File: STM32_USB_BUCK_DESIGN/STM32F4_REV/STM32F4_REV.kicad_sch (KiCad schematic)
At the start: 5 parts

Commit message: work going on ckt-desgin
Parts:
- added C? (x5): 100n, symbol Device:C_Small
- added C?: 4u7, symbol Device:C_Small
- added C?: 1u, symbol Device:C_Small
- added C? (x2): 12pF, symbol Device:C_Small
- added C?: 1n, symbol Device:C_Small
- added D?: LED, symbol Device:LED
- added L?: 39h, symbol pspice:INDUCTOR
- added R?: 47, symbol Device:R_Small
- added R?: 1K5, symbol Device:R_Small
- added U?: mp2359, symbol Prashant_library:mp2359
- added Y?: 16Mhz, symbol Device:Crystal_GND24_Small
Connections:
- net +3.3V: now also C?.1, C?.1, C?.1, C?.1, C?.1, C?.1, L?.1
- net GND: now also C?.2, C?.2, C?.2, C?.2, C?.2, C?.2, C?.2, C?.2, C?.2, C?.2, D?.1 (K), U?.2 (GND), Y?.2, Y?.4
- net HSE_IN: now also C?.1, Y?.1
- net HSE_ON: now also R?.1
- net LED_STATUS: now also R?.1
- new net: C?.1, R?.2, Y?.3
- new net: D?.2 (A), R?.2
- new net +3.3VA: C?.1, C?.1, L?.2
- new net BUCK_BST: U?.1 (BST)
- new net BUCK_EN: U?.4 (EN)
- new net BUCK_FB: U?.3 (FB)
- new net BUCK_IN: U?.5 (IN)
- new net BUCK_SW: U?.6 (SW)
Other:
- note added: "CLoad = 2*(CL - Cstray)"
- moved on the sheet: R?, SW?

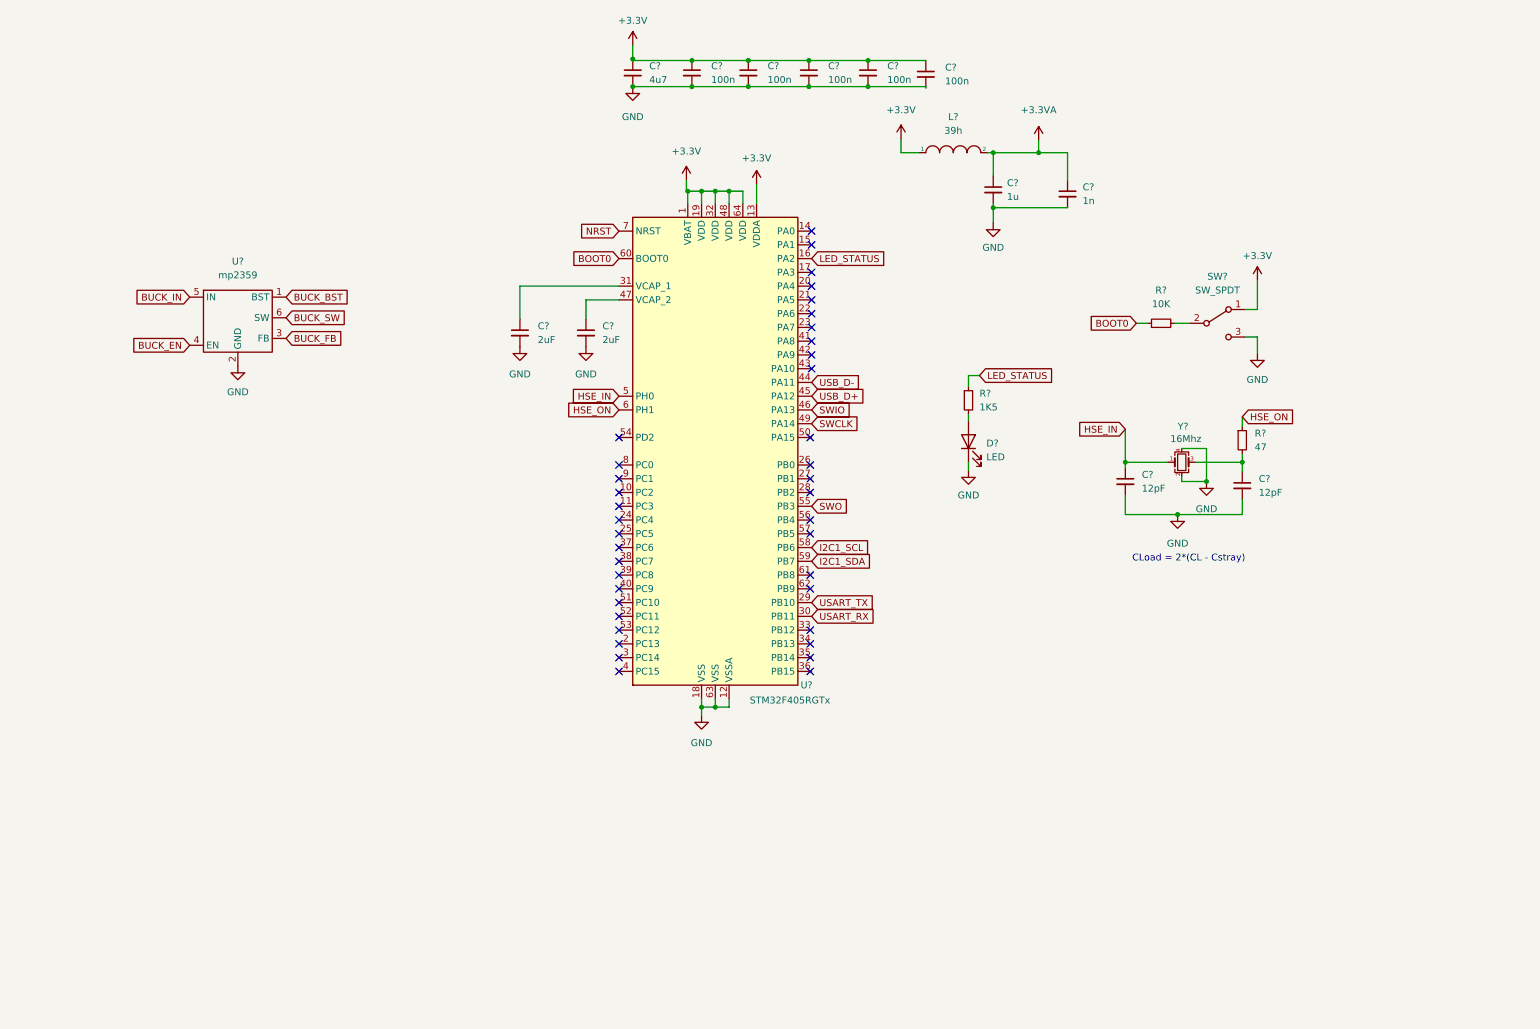
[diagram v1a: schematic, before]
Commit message: design of STM32_USB_BUCK_DESIGN
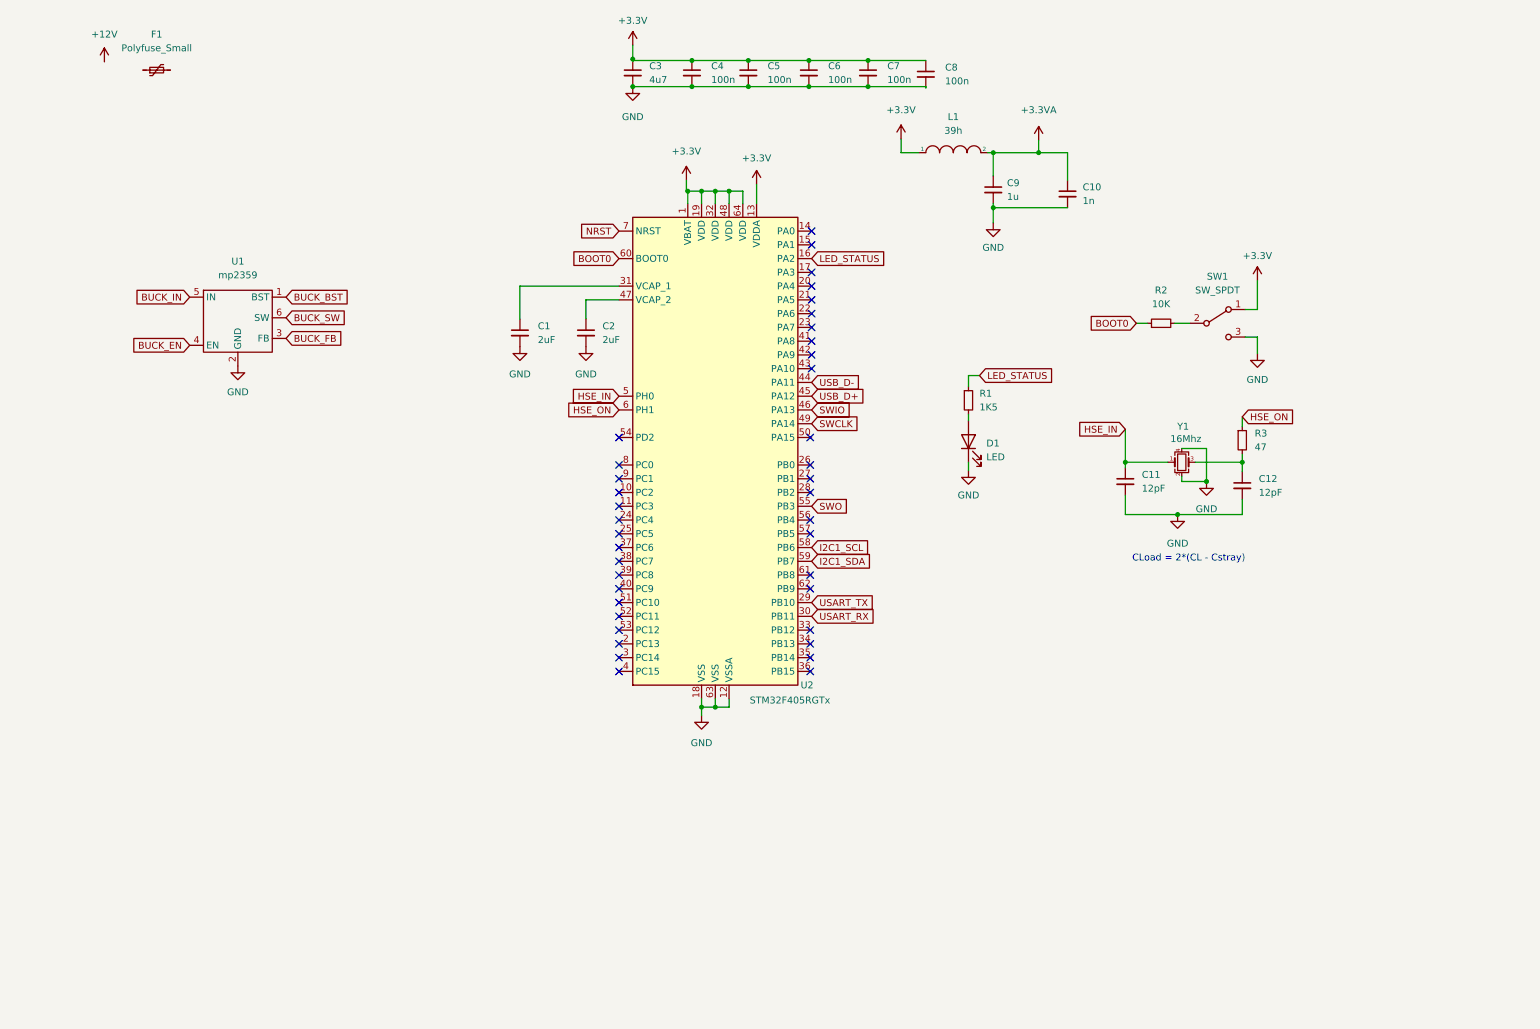
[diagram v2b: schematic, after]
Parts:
- added F1: Polyfuse_Small, symbol Device:Polyfuse_Small
- gave numbers to parts that had none: 21

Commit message: Kam vairaxa
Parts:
- added C1, C2, C3: 10u, Capacitor_SMD:C_1206_3216Metric, symbol Device:C_Small
- added C4: 10n, Capacitor_SMD:C_0603_1608Metric, symbol Device:C_Small
- added D1, D2, D3: B5819W, Diode_SMD:D_SOD-123, symbol Device:D_Schottky_Small
- added D5: LED_Small, LED_SMD:LED_0603_1608Metric, symbol Device:LED_Small
- added FB1: 600 @ 600 MHz, Inductor_SMD:L_0805_2012Metric, symbol Device:FerriteBead_Small
- added H1, H2, H3, H4: MountingHole_Pad, MountingHole:MountingHole_4.3mm_M4_Pad_Via, symbol Mechanical:MountingHole_Pad
- added J1: USB_B_Micro, Connector_USB:USB_Micro-B_Amphenol_10104110_Horizontal, symbol Connector:USB_B_Micro
- added J2: Screw_Terminal_01x02, TerminalBlock_Phoenix:TerminalBlock_Phoenix_PT-1,5-2-3.5-H_1x02_P3.50mm_Horizontal, symbol Connector:Screw_Terminal_01x02
- added J3, J5: Conn_01x04, Connector_Molex:Molex_PicoBlade_53048-0410_1x04_P1.25mm_Horizontal, symbol Connector_Generic:Conn_01x04
- added J4: Conn_02x05_Odd_Even, Connector_PinSocket_1.27mm:PinSocket_2x05_P1.27mm_Vertical_SMD, symbol Connector_Generic:Conn_02x05_Odd_Even
- added L2: 10u, symbol Device:L_Small
- added R10: 270, symbol Device:R_Small
- added R11: 1K, symbol Device:R_Small
- added R4: 100K, symbol Device:R_Small
- added R5: 68K, symbol Device:R_Small
- added R6, R7: 2K2, symbol Device:R_Small
- added R8: 47K, symbol Device:R_Small
- added R9: 15K, symbol Device:R_Small
- added U3: USBLC6-2SC6, Package_TO_SOT_SMD:SOT-23-6, symbol Power_Protection:USBLC6-2SC6
- C10: renamed from C8; footprint (none) -> Capacitor_SMD:C_0603_1608Metric
- C11: renamed from C9; footprint (none) -> Capacitor_SMD:C_0603_1608Metric
- C12: renamed from C10; footprint (none) -> Capacitor_SMD:C_0603_1608Metric
- C13: renamed from C1; value 2uF -> 2u2; footprint (none) -> Capacitor_SMD:C_0603_1608Metric
- C14: renamed from C2; value 2uF -> 2u2; footprint (none) -> Capacitor_SMD:C_0603_1608Metric
- C15: renamed from C11; footprint (none) -> Capacitor_SMD:C_0805_2012Metric
- C16: renamed from C12; footprint (none) -> Capacitor_SMD:C_0805_2012Metric
- C5: renamed from C3; footprint (none) -> Capacitor_SMD:C_0805_2012Metric
- C6: renamed from C4; footprint (none) -> Capacitor_SMD:C_0603_1608Metric
- C7: renamed from C5; footprint (none) -> Capacitor_SMD:C_0603_1608Metric
- C8: renamed from C6; footprint (none) -> Capacitor_SMD:C_0603_1608Metric
- C9: renamed from C7; footprint (none) -> Capacitor_SMD:C_0603_1608Metric
- D4: renamed from D1; footprint (none) -> LED_SMD:LED_0603_1608Metric
- F1: footprint (none) -> Fuse:Fuse_1206_3216Metric
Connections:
- net +12V: now also F1.1, J2.1 (Pin_1)
- net +3.3V: now also C2.1, C3.1, D5.1 (K), J3.1 (Pin_1), J4.1 (Pin_1), J5.1 (Pin_1), L2.2, R6.1, R7.1, R8.1
- net BUCK_BST: now also C4.1
- net BUCK_EN: now also R4.2, R5.1
- net BUCK_FB: now also R8.2, R9.1
- net BUCK_IN: now also C1.1, FB1.2, R4.1
- net BUCK_SW: now also C4.2, D3.1 (K), L2.1
- net GND: now also C1.2, C2.2, C3.2, D3.2 (A), H1.1, H2.1, H3.1, H4.1, J1.5 (GND), J2.2 (Pin_2), J3.4 (Pin_4), J4.3 (Pin_3), J4.5 (Pin_5), J4.9 (Pin_9), J5.4 (Pin_4), R10.2, R11.2, R5.2, U3.2 (GND)
- net I2C1_SCL: now also J3.2 (Pin_2), R6.2
- net I2C1_SDA: now also J3.3 (Pin_3), R7.2
- net NRST: now also J4.10 (Pin_10)
- net SWCLK: now also J4.4 (Pin_4)
- net SWO: now also J4.6 (Pin_6)
- net USART_RX: now also J5.3 (Pin_3)
- net USART_TX: now also J5.2 (Pin_2)
- net USB_D+: now also U3.4 (I/O2)
- net USB_D-: now also U3.6 (I/O1)
- net at F1.2: now also D1.2 (A)
- net SWIO renamed SWDIO
- net SWDIO: now also J4.2 (Pin_2)
- new net: R10.1, R9.2
- new net: D5.2 (A), R11.1
- new net: D1.1 (K), D2.1 (K), FB1.1
- new net +5V: D2.2 (A), J1.1 (VBUS), U3.5 (VBUS)
- new net USB_Conn_D+: J1.3 (D+), U3.3 (I/O2)
- new net USB_Conn_D-: J1.2 (D-), U3.1 (I/O1)
- no-connect marks 39 -> 43
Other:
- note added: "2.2 4.7 or 10K any value would be good under the conditions for pullup high"
- note added: "Microcontroller Section"
- note added: "Power Circuitry Section"
- moved on the sheet: C10, C11, C12, C13, C14, C15, C16, C5, C6, C7, C8, C9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
